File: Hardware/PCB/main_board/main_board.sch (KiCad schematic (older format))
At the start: 0 parts

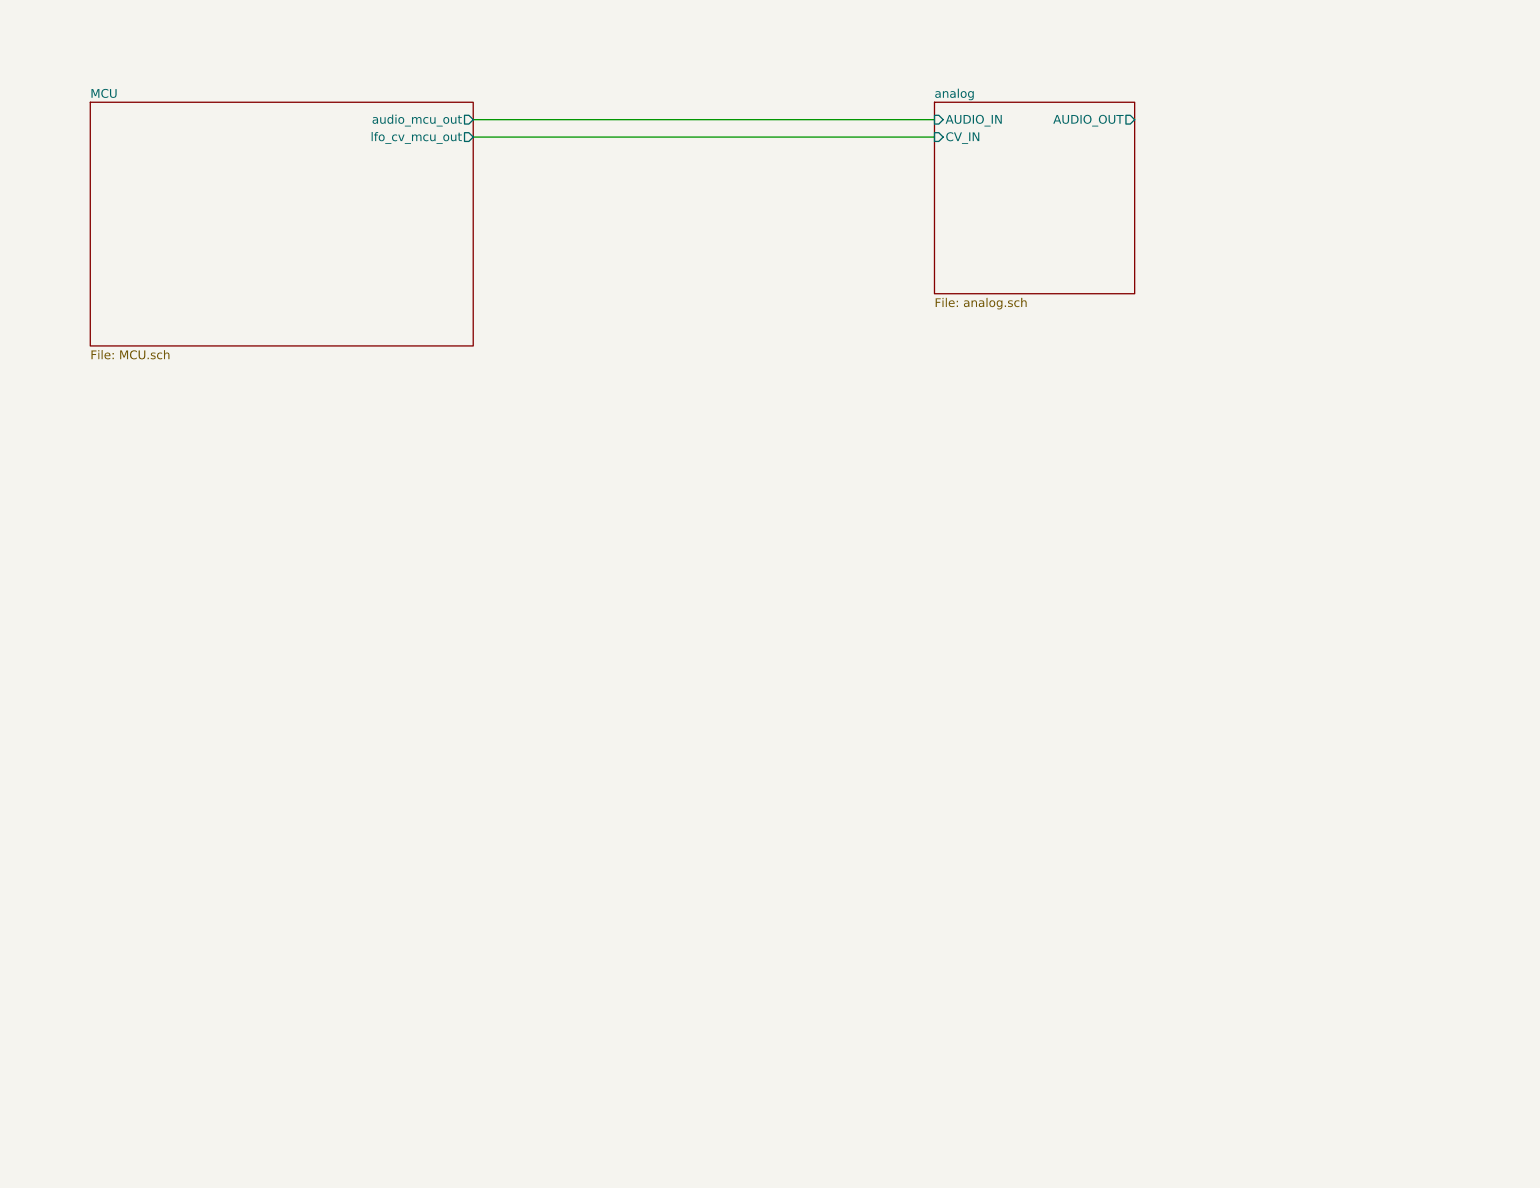
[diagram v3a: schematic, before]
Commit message: Add MIDI hardware
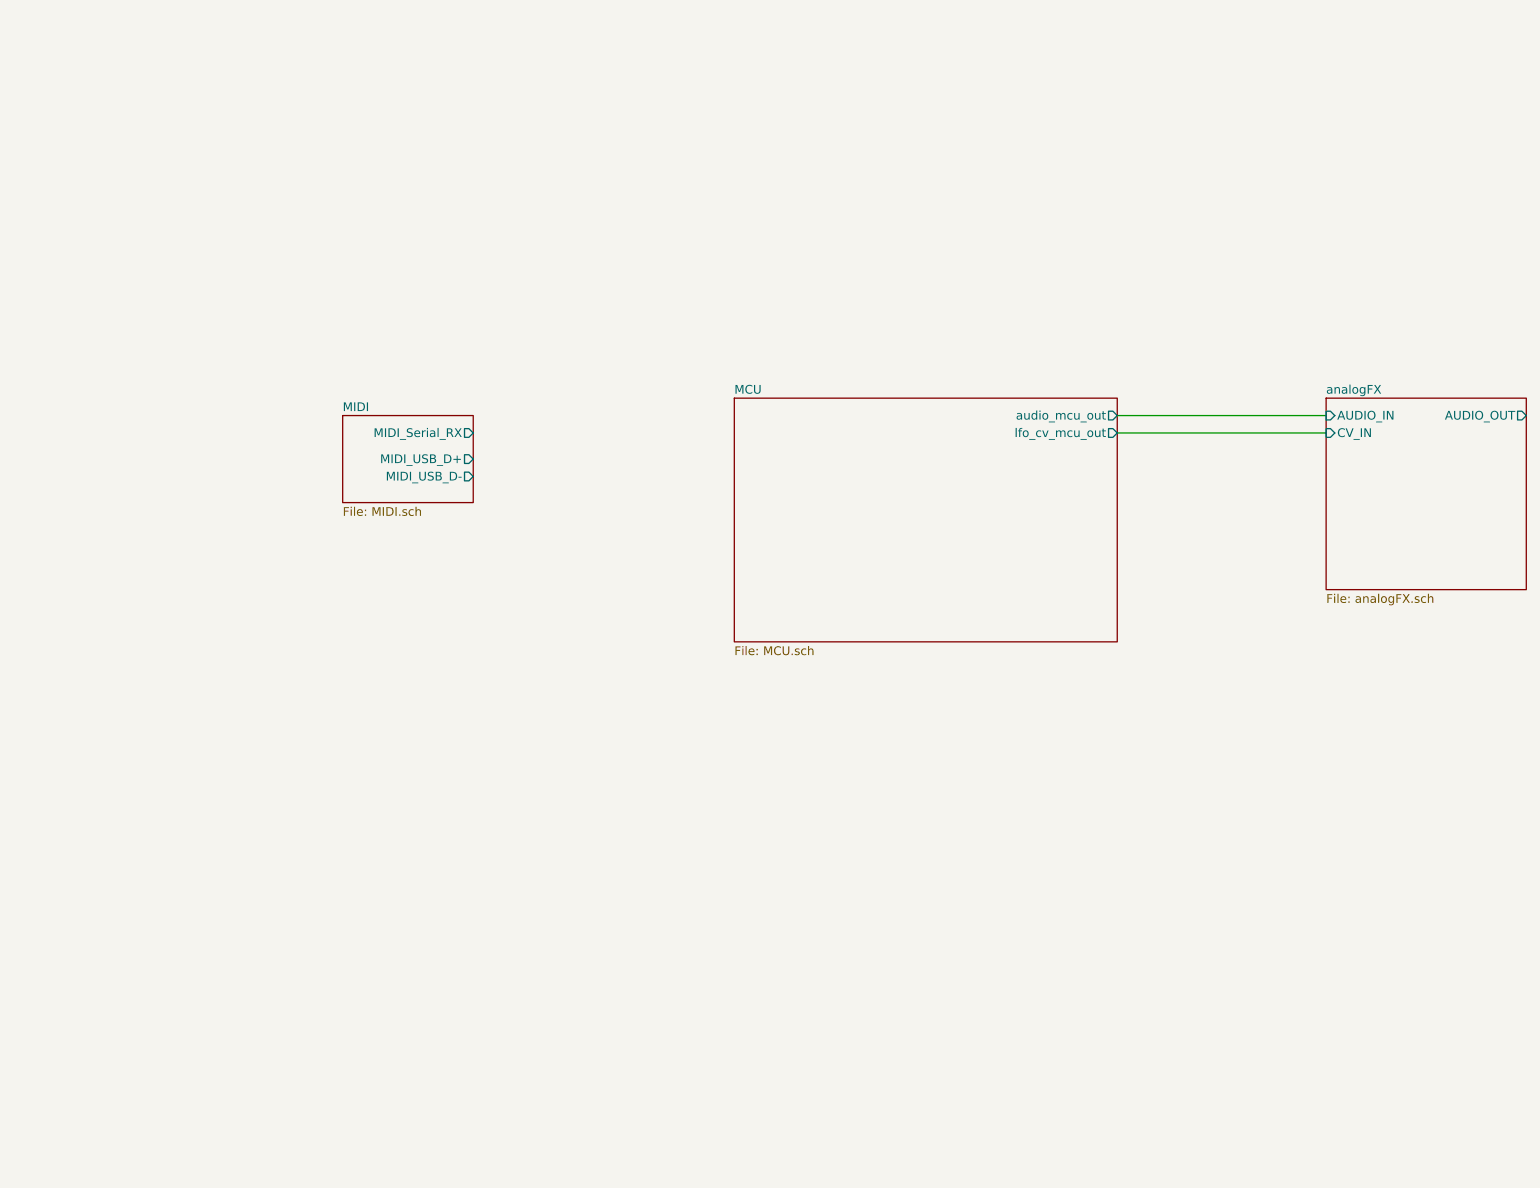
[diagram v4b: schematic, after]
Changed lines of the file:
@@
 $Descr A4 11693 8268
 encoding utf-8
-Sheet 1 3
+Sheet 1 4
 Title ""
 Date ""
@@
 $EndDescr
 $Sheet
-S 5900 1150 1150 1100
-U 5E632F77
-F0 "analog" 50
-F1 "analog.sch" 50
-F2 "AUDIO_OUT" O R 7050 1250 50
-F3 "CV_IN" I L 5900 1350 50
-F4 "AUDIO_IN" I L 5900 1250 50
-$EndSheet
-$Sheet
-S 1050 1150 2200 1400
+S 4750 2850 2200 1400
 U 5E658709
 F0 "MCU" 50
 F1 "MCU.sch" 50
-F2 "audio_mcu_out" O R 3250 1250 50
-F3 "lfo_cv_mcu_out" O R 3250 1350 50
+F2 "audio_mcu_out" O R 6950 2950 50
+F3 "lfo_cv_mcu_out" O R 6950 3050 50
 $EndSheet
 Wire Wire Line
-	3250 1250 5900 1250
+	6950 2950 8150 2950
 Wire Wire Line
-	3250 1350 5900 1350
+	6950 3050 8150 3050
+$Sheet
+S 2500 2950 750  500
+U 5E513BF6
+F0 "MIDI" 50
+F1 "MIDI.sch" 50
+F2 "MIDI_Serial_RX" O R 3250 3050 50
+F3 "MIDI_USB_D+" O R 3250 3200 50
+F4 "MIDI_USB_D-" O R 3250 3300 50
+$EndSheet
+$Sheet
+S 8150 2850 1150 1100
+U 5E632F77
+F0 "analogFX" 50
+F1 "analogFX.sch" 50
+F2 "AUDIO_OUT" O R 9300 2950 50
+F3 "CV_IN" I L 8150 3050 50
+F4 "AUDIO_IN" I L 8150 2950 50
+$EndSheet
 $EndSCHEMATC

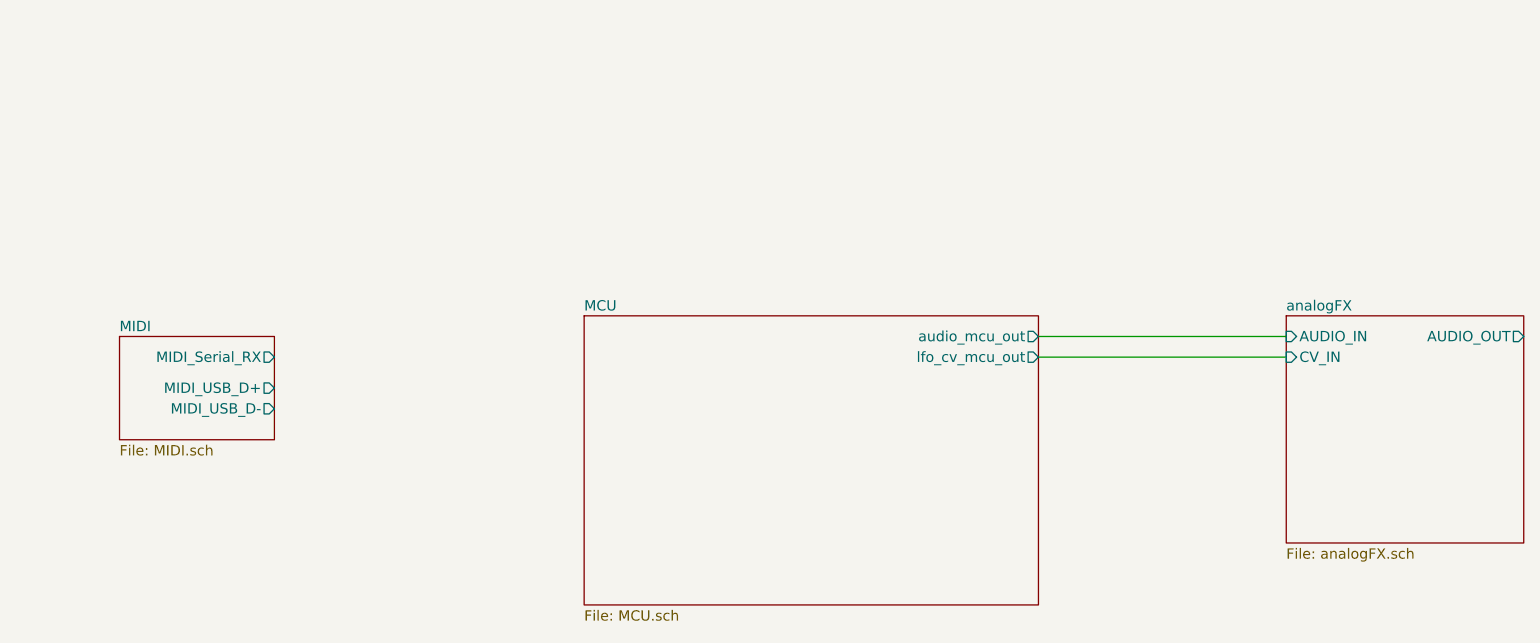
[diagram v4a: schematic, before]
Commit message: Add power supply schematics and layout
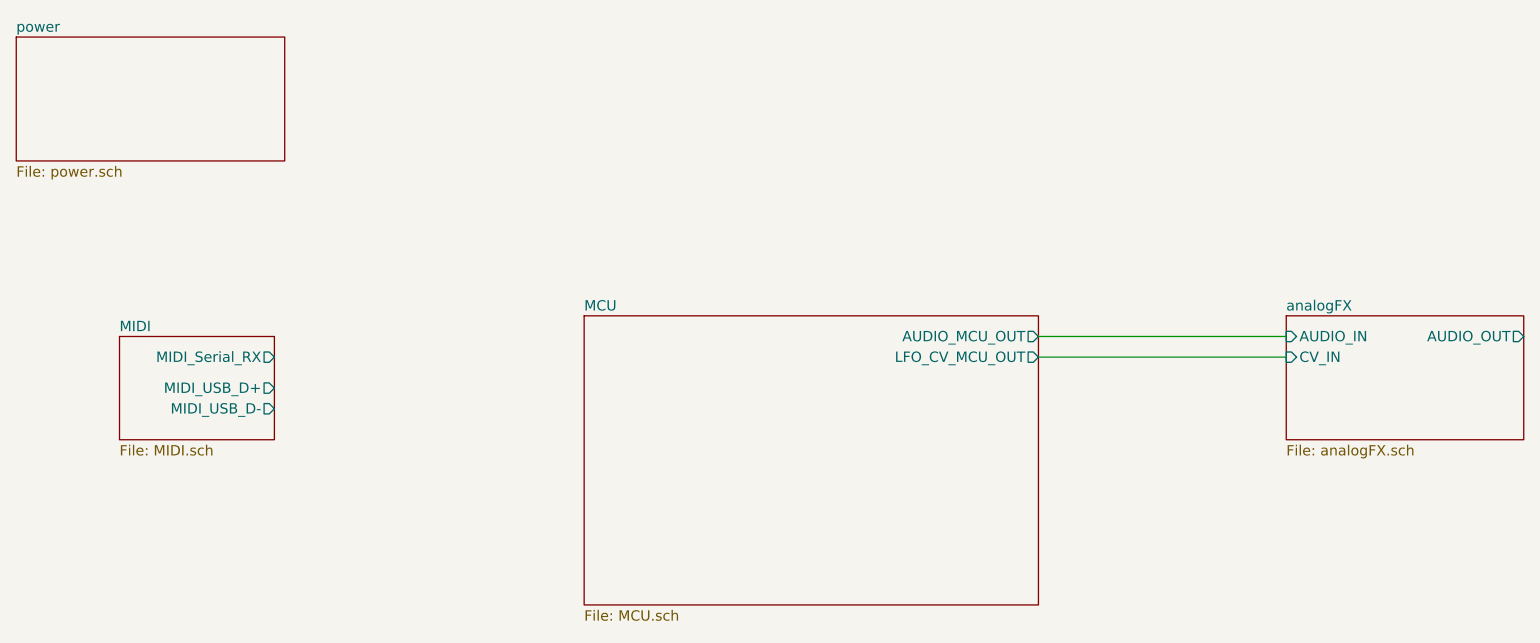
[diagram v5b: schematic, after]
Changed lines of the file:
@@
 $Descr A4 11693 8268
 encoding utf-8
-Sheet 1 4
+Sheet 1 5
 Title ""
 Date ""
@@
 Comment4 ""
 $EndDescr
-$Sheet
-S 4750 2850 2200 1400
-U 5E658709
-F0 "MCU" 50
-F1 "MCU.sch" 50
-F2 "audio_mcu_out" O R 6950 2950 50
-F3 "lfo_cv_mcu_out" O R 6950 3050 50
-$EndSheet
 Wire Wire Line
 	6950 2950 8150 2950
@@
 $EndSheet
 $Sheet
-S 8150 2850 1150 1100
+S 8150 2850 1150 600
 U 5E632F77
 F0 "analogFX" 50
@@
 F4 "AUDIO_IN" I L 8150 2950 50
 $EndSheet
+$Sheet
+S 4750 2850 2200 1400
+U 5E658709
+F0 "MCU" 50
+F1 "MCU.sch" 50
+F2 "AUDIO_MCU_OUT" O R 6950 2950 50
+F3 "LFO_CV_MCU_OUT" O R 6950 3050 50
+$EndSheet
+$Sheet
+S 2000 1500 1300 600
+U 5E57C92D
+F0 "power" 50
+F1 "power.sch" 50
+$EndSheet
 $EndSCHEMATC

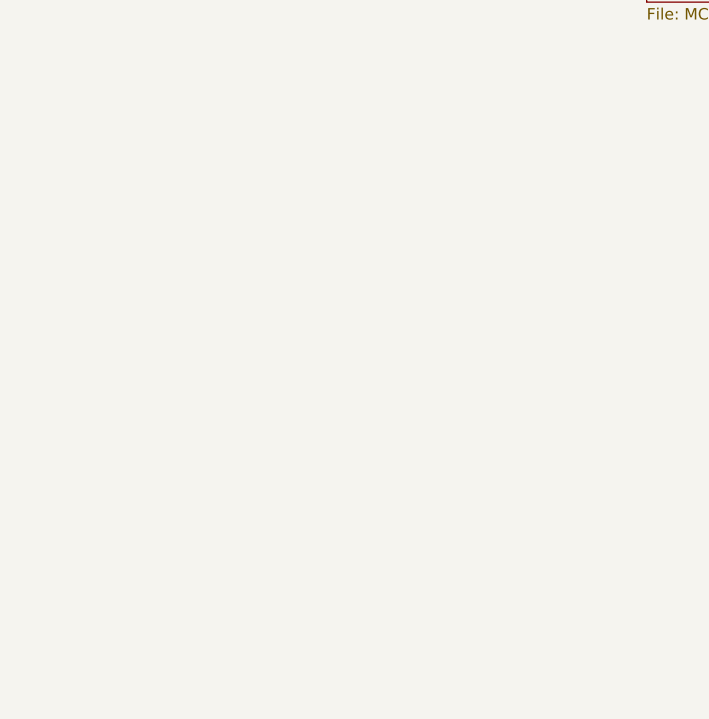
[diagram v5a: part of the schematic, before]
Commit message: Add OLED screen to PCB
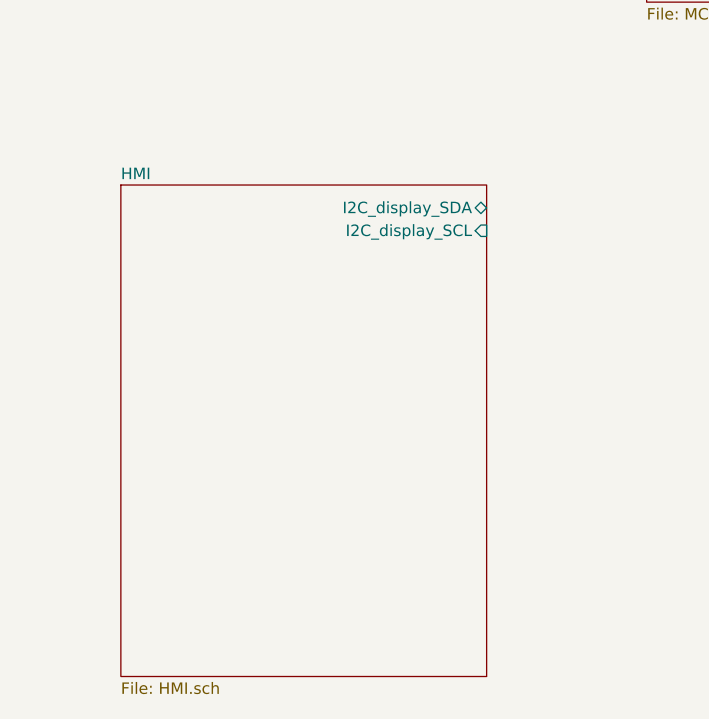
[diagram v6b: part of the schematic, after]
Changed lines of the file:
@@
 $Descr A4 11693 8268
 encoding utf-8
-Sheet 1 5
+Sheet 1 6
 Title ""
 Date ""
@@
 F1 "power.sch" 50
 $EndSheet
+$Sheet
+S 2450 5050 1600 2150
+U 5E525BAF
+F0 "HMI" 50
+F1 "HMI.sch" 50
+F2 "I2C_display_SDA" B R 4050 5150 50
+F3 "I2C_display_SCL" I R 4050 5250 50
+$EndSheet
 $EndSCHEMATC
